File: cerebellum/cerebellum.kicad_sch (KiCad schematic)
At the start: 78 parts, among them J1 PowerIn, J2 UART, J3 SWD_DBG, J4 SWD_DBG_PIN, J5 CAN FD, J6 CAN, Q1 AP2300, U1 OK1061-S, U2 TPS5430DDA, U3 BMI088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

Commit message: [Modify] Complete descriptions in schematics
including cerebellum and heart.
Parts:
- C1, C10, C2, C27, C30, C32, C38, C5, C51, C7: value 100nF, 10%, 10V -> 100nF/10V/0402
- C11, C22, C23, C9: value 100pF, 10%, 10V -> 100pF/1%/50V/0402
- C12, C29, C3, C31, C8: value 4.7uF, 10%, 10V -> 4.7uF/10V/0402
- C13, C16, C18: value 4.7uF 50V -> 4.7uF/50V/0805
- C14: value 10pf 50V -> 10pf/50V/0402
- C15: value 1.5nf 50V -> 1.5nf/50V/0603
- C17: value 10nf 50V -> 10nf/50V/0402
- C19: value 100uf 50V -> 100uf/50V/0805
- C20: value 100nf 10V -> 100nf/10V/0402
- C21: value 1.5nf 50V -> 1.5nf/50V/0402
- C24: value 100nf 50V -> 100nf/50V/0402
- C25: value 10uf 50V -> 10uf/50V/0402
- C26: value 8.2nf 50V -> 8.2nf/50V/0603
- C28: value 150pf 50V -> 150pf/50V/0402
- C33, C36: value 47uf 50V -> 47uf/50V/0603
- C4: value 1uF, 10%, 10V -> 1uF/10V/0402
- C6: value 10uF, 10%, 10V -> 10uF/10V/0402
- D5: value LTST-C281KFKT-5A -> LTST-C281KFKT-5A/0402
- L1, L2, L3: value 15uh, SLO0530H150MTT -> 15uh/SLO0530H150MTT
- R1: value 1k -> 1k/0402
- R10, R6: value 10k -> 10k/0402
- R11: value 549R -> 549R/0201
- R12, R13, R14, R15: value 33R/1% -> 33R/1%/0805
- R16: value 10.2k -> 10.2k/0402
- R17: value 1.96k -> 1.96k/0402
- R2, R8: value 120R -> 120R/0402
- R3: value 64.9k -> 64.9k/0402
- R4: value 169k -> 169k/0402
- R5: value 20.5 -> 20.5/0402
- R7: value 5.9k -> 5.9k/0402
- R9: value 100R -> 100R/0402

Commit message: [Fix] Complete resistor value of 24Vto5V regulator
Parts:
- R5: value 20.5/0402 -> 20.5k/0402
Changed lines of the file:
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@@
       (effects (font (size 1.27 1.27)) (justify right))
     )
-    (property "Value" "20.5/0402" (id 1) (at 294.64 123.19 0)
+    (property "Value" "20.5k/0402" (id 1) (at 294.64 123.19 0)
       (effects (font (size 1.27 1.27)) (justify right))
     )
@@
     )
     (path "/242cc630-7b5d-45c5-9414-a0c5ca6aa299"
-      (reference "R5") (unit 1) (value "20.5/0402") (footprint "Resistor_SMD:R_0402_1005Metric")
+      (reference "R5") (unit 1) (value "20.5k/0402") (footprint "Resistor_SMD:R_0402_1005Metric")
     )
     (path "/f57f7c10-af7d-4f52-88fd-8d7ce55973b5"

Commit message: [Fix] Correct capacities in 24Vto5V converter
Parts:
- C25: value 10uf/50V/0402 -> 10uf/50V/0805; footprint Capacitor_SMD:C_0402_1005Metric -> Capacitor_SMD:C_0805_2012Metric
- C33, C36: value 47uf/50V/0603 -> 47uf/6.3V/0603
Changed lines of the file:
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@@
       (effects (font (size 1.27 1.27)) (justify left))
     )
-    (property "Value" "47uf/50V/0603" (id 1) (at 363.22 124.46 90)
+    (property "Value" "47uf/6.3V/0603" (id 1) (at 363.22 124.46 90)
       (effects (font (size 1.27 1.27)) (justify left))
     )
@@
   (symbol (lib_id "power:GNDA") (at 92.71 77.47 0) (unit 1)
     (in_bom yes) (on_board yes)
-    (property "Reference" "#PWR?" (id 0) (at 92.71 83.82 0)
+    (property "Reference" "#PWR0110" (id 0) (at 92.71 83.82 0)
       (effects (font (size 1.27 1.27)) hide)
     )
@@
       (effects (font (size 1.27 1.27)) (justify left))
     )
-    (property "Value" "47uf/50V/0603" (id 1) (at 370.84 124.46 90)
+    (property "Value" "47uf/6.3V/0603" (id 1) (at 370.84 124.46 90)
       (effects (font (size 1.27 1.27)) (justify left))
     )
@@
       (effects (font (size 1.27 1.27)) (justify left))
     )
-    (property "Value" "10uf/50V/0402" (id 1) (at 283.21 119.38 90)
-      (effects (font (size 1.27 1.27)) (justify left))
-    )
-    (property "Footprint" "Capacitor_SMD:C_0402_1005Metric" (id 2) (at 287.9852 114.3 0)
+    (property "Value" "10uf/50V/0805" (id 1) (at 283.21 119.38 90)
+      (effects (font (size 1.27 1.27)) (justify left))
+    )
+    (property "Footprint" "Capacitor_SMD:C_0805_2012Metric" (id 2) (at 287.9852 114.3 0)
       (effects (font (size 1.27 1.27)) hide)
     )
@@
     )
     (path "/55191d87-ff63-48e6-b782-b5eabc48b1c7"
-      (reference "#PWR?") (unit 1) (value "GNDA") (footprint "")
+      (reference "#PWR0110") (unit 1) (value "GNDA") (footprint "")
     )
     (path "/65313aad-28bf-4519-8673-ecacf3cd8ac6"
@@
     )
     (path "/e787b22a-3d91-4a17-98b9-353fe0181fec"
-      (reference "C25") (unit 1) (value "10uf/50V/0402") (footprint "Capacitor_SMD:C_0402_1005Metric")
+      (reference "C25") (unit 1) (value "10uf/50V/0805") (footprint "Capacitor_SMD:C_0805_2012Metric")
     )
     (path "/93be202b-fdc3-4e76-b2fd-15b6cdae9e2f"
@@
     )
     (path "/0ddd73d0-49e9-4519-8799-16055b6184fb"
-      (reference "C33") (unit 1) (value "47uf/50V/0603") (footprint "Capacitor_SMD:C_0603_1608Metric")
+      (reference "C33") (unit 1) (value "47uf/6.3V/0603") (footprint "Capacitor_SMD:C_0603_1608Metric")
     )
     (path "/d3316d42-63af-4c88-8de1-8da058897181"
-      (reference "C36") (unit 1) (value "47uf/50V/0603") (footprint "Capacitor_SMD:C_0603_1608Metric")
+      (reference "C36") (unit 1) (value "47uf/6.3V/0603") (footprint "Capacitor_SMD:C_0603_1608Metric")
     )
     (path "/0ee1750c-811c-4543-bb64-0d4b8ab140a1"

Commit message: [Modify] Change CAN ports sequence
2pin: 1-CAN_L, 2-CAN_H
3pin: 1-5V, 2-CAN_L, 3-CAN_H
4pin: 1,2-CAN_L, 3,4-CAN_H

Signed-off-by: Homalozoa <nx.tardis@gmail.com>
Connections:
- net CANFD_H: now also J5.2 (Pin_2); no longer J5.1 (Pin_1)
- net CANFD_L: now also J5.1 (Pin_1); no longer J5.2 (Pin_2)
- net CAN_H: now also J6.2 (Pin_2); no longer J6.1 (Pin_1)
- net CAN_L: now also J6.1 (Pin_1); no longer J6.2 (Pin_2)

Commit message: [Fix] Manufacture modification
Signed-off-by: Homalozoa <nx.tardis@gmail.com>
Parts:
- C19: value 100uf/50V/0805 -> 100uf/6.3V/0805
- D3, D4, D6, D7: value 12V -> BV12C
- R11: value 549R/0201 -> 549R/0603; footprint Resistor_SMD:R_0201_0603Metric -> Resistor_SMD:R_0603_1608Metric
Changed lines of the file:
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@@
     (in_bom yes) (on_board yes)
     (property "Reference" "C19" (id 0) (at 334.01 50.8 0))
-    (property "Value" "100uf/50V/0805" (id 1) (at 336.55 55.88 0))
+    (property "Value" "100uf/6.3V/0805" (id 1) (at 336.55 55.88 0))
     (property "Footprint" "Capacitor_SMD:C_0805_2012Metric" (id 2) (at 330.5048 49.53 0)
       (effects (font (size 1.27 1.27)) hide)
@@
       (effects (font (size 1.27 1.27)) (justify right))
     )
-    (property "Value" "12V" (id 1) (at 208.28 238.76 90)
+    (property "Value" "BV12C" (id 1) (at 208.28 238.76 90)
       (effects (font (size 1.27 1.27)) (justify right))
     )
@@
   (symbol (lib_id "Device:R_US") (at 379.73 57.15 0) (mirror y) (unit 1)
     (in_bom yes) (on_board yes) (fields_autoplaced)
-    (property "Reference" "R11" (id 0) (at 377.19 55.8799 0)
-      (effects (font (size 1.27 1.27)) (justify left))
-    )
-    (property "Value" "549R/0201" (id 1) (at 377.19 58.4199 0)
-      (effects (font (size 1.27 1.27)) (justify left))
-    )
-    (property "Footprint" "Resistor_SMD:R_0201_0603Metric" (id 2) (at 378.714 57.404 90)
+    (property "Reference" "R11" (id 0) (at 382.27 55.8799 0)
+      (effects (font (size 1.27 1.27)) (justify right))
+    )
+    (property "Value" "549R/0603" (id 1) (at 382.27 58.4199 0)
+      (effects (font (size 1.27 1.27)) (justify right))
+    )
+    (property "Footprint" "Resistor_SMD:R_0603_1608Metric" (id 2) (at 378.714 57.404 90)
       (effects (font (size 1.27 1.27)) hide)
     )
@@
       (effects (font (size 1.27 1.27)) (justify right))
     )
-    (property "Value" "12V" (id 1) (at 190.5 227.33 90)
+    (property "Value" "BV12C" (id 1) (at 190.5 227.33 90)
       (effects (font (size 1.27 1.27)) (justify right))
     )
@@
       (effects (font (size 1.27 1.27)) (justify right))
     )
-    (property "Value" "12V" (id 1) (at 123.19 226.06 90)
+    (property "Value" "BV12C" (id 1) (at 123.19 226.06 90)
       (effects (font (size 1.27 1.27)) (justify right))
     )
@@
       (effects (font (size 1.27 1.27)) (justify right))
     )
-    (property "Value" "12V" (id 1) (at 140.97 237.49 90)
+    (property "Value" "BV12C" (id 1) (at 140.97 237.49 90)
       (effects (font (size 1.27 1.27)) (justify right))
     )
@@
     )
     (path "/0f6c3a96-c6a2-4cae-b238-f3f5c233b895"
-      (reference "C19") (unit 1) (value "100uf/50V/0805") (footprint "Capacitor_SMD:C_0805_2012Metric")
+      (reference "C19") (unit 1) (value "100uf/6.3V/0805") (footprint "Capacitor_SMD:C_0805_2012Metric")
     )
     (path "/1a81ed92-b7d6-4e2e-b1fa-f759489fe3e3"
@@
     )
     (path "/d6cf48a9-a13f-466f-bfde-8bc93913d1c0"
-      (reference "D3") (unit 1) (value "12V") (footprint "Diode_SMD:D_SOD-323")
+      (reference "D3") (unit 1) (value "BV12C") (footprint "Diode_SMD:D_SOD-323")
     )
     (path "/dca75d67-8d31-4cfe-944d-9a96274d2c81"
-      (reference "D4") (unit 1) (value "12V") (footprint "Diode_SMD:D_SOD-323")
+      (reference "D4") (unit 1) (value "BV12C") (footprint "Diode_SMD:D_SOD-323")
     )
     (path "/a30c0642-d8e5-452a-8e07-4ec5af02c9d7"
@@
     )
     (path "/35231abb-451c-4485-8adf-5fdeff949361"
-      (reference "D6") (unit 1) (value "12V") (footprint "Diode_SMD:D_SOD-323")
+      (reference "D6") (unit 1) (value "BV12C") (footprint "Diode_SMD:D_SOD-323")
     )
     (path "/28d5a148-bc54-44f3-9073-42e0716c8823"
-      (reference "D7") (unit 1) (value "12V") (footprint "Diode_SMD:D_SOD-323")
+      (reference "D7") (unit 1) (value "BV12C") (footprint "Diode_SMD:D_SOD-323")
     )
     (path "/21df13e8-f1cb-4d93-9100-820a610e89e4"
@@
     )
     (path "/2f096358-cf9a-4b82-969d-9875d4f6edad"
-      (reference "R11") (unit 1) (value "549R/0201") (footprint "Resistor_SMD:R_0201_0603Metric")
+      (reference "R11") (unit 1) (value "549R/0603") (footprint "Resistor_SMD:R_0603_1608Metric")
     )
     (path "/8ef88884-2b22-48df-9a58-892a579574e1"

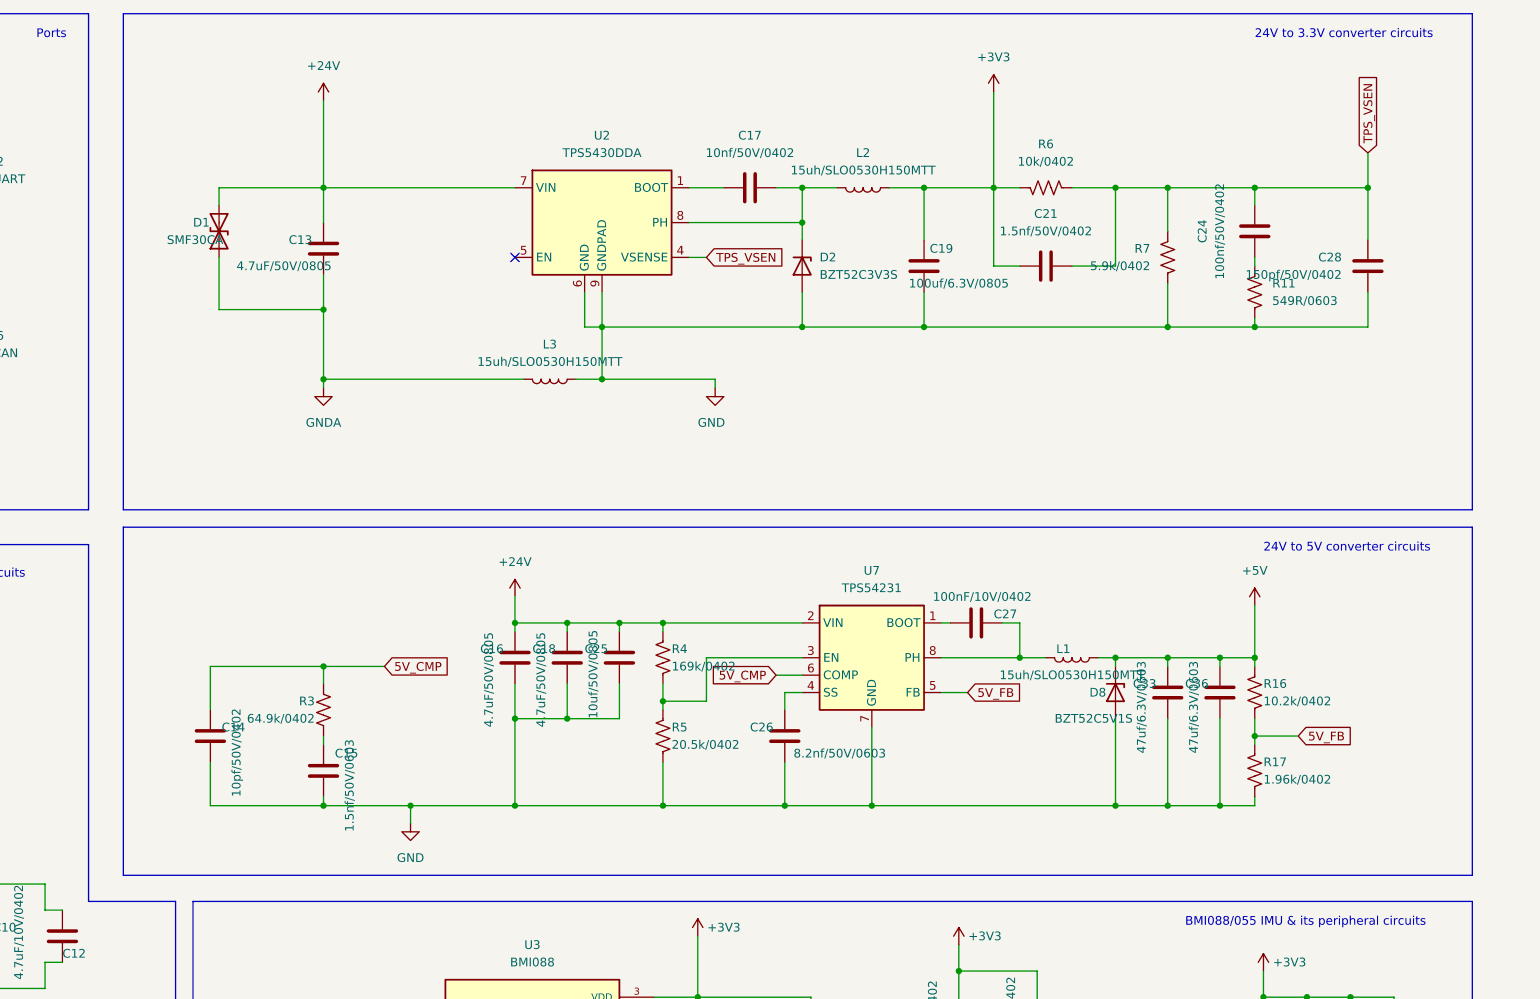
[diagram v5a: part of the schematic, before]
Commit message: [Modify] Replace DCDC(24to3V3) to LDO(5to3V3)
Signed-off-by: Homalozoa <nx.tardis@gmail.com>
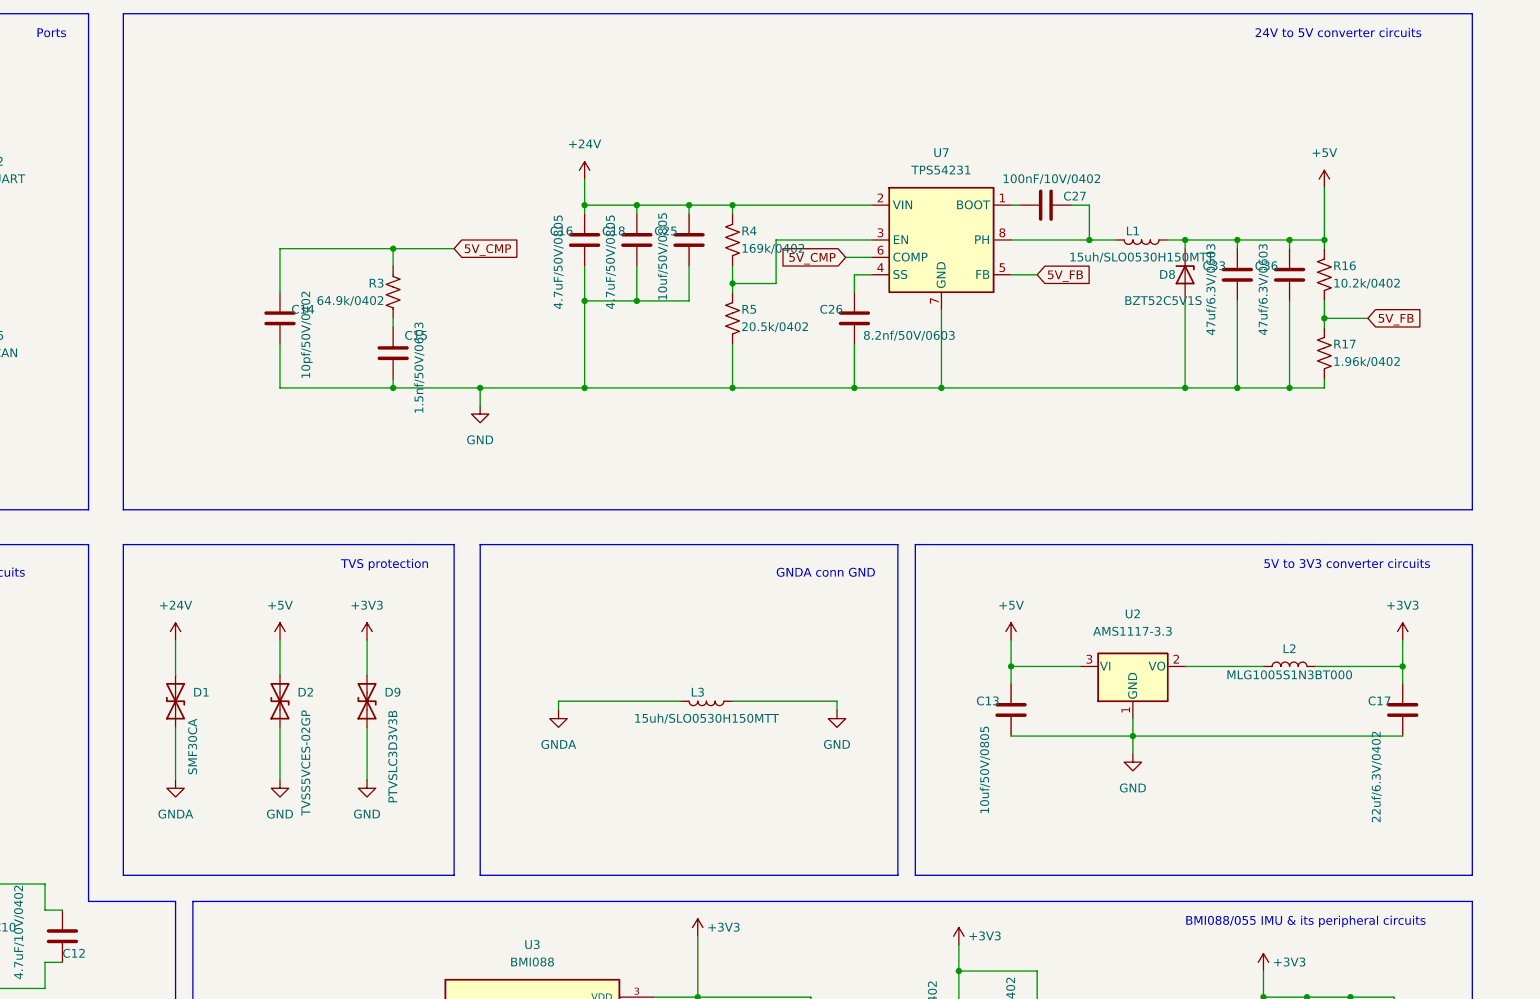
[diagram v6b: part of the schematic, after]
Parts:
- removed C19: 100uf/6.3V/0805, Capacitor_SMD:C_0805_2012Metric, symbol Device:C
- removed C21: 1.5nf/50V/0402, Capacitor_SMD:C_0402_1005Metric, symbol Device:C
- removed C24: 100nf/50V/0402, Capacitor_SMD:C_0402_1005Metric, symbol Device:C
- removed C28: 150pf/50V/0402, Capacitor_SMD:C_0402_1005Metric, symbol Device:C
- removed D2: BZT52C3V3S, Diode_SMD:D_SOD-323, symbol Diode:BZT52Bxx
- removed R11: 549R/0603, Resistor_SMD:R_0603_1608Metric, symbol Device:R_US
- removed R6: 10k/0402, Resistor_SMD:R_0402_1005Metric, symbol Device:R_US
- removed R7: 5.9k/0402, Resistor_SMD:R_0402_1005Metric, symbol Device:R_US
- removed U2: TPS5430DDA, Package_SO:TI_SO-PowerPAD-8_ThermalVias, symbol Regulator_Switching:TPS5430DDA
- added D2: TVSS5VCES-02GP, Diode_SMD:D_SOD-523, symbol Device:D_TVS
- added D9: PTVSLC3D3V3B, Diode_SMD:D_SOD-323, symbol Device:D_TVS
- added U2: AMS1117-3.3, Package_TO_SOT_SMD:SOT-223-3_TabPin2, symbol Regulator_Linear:AMS1117-3.3
- C13: value 4.7uF/50V/0805 -> 10uf/50V/0805
- C17: value 10nf/50V/0402 -> 22uf/6.3V/0402
- L2: value 15uh/SLO0530H150MTT -> MLG1005S1N3BT000; footprint Inductor_SMD:L_Sunlord_MWSA0518_5.4x5.2mm -> Inductor_SMD:L_0402_1005Metric
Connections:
- net +24V: no longer C13.1
- net +3V3: now also C17.1, L2.2, D9.2 (A2); no longer L2.1
- net +5V: now also C13.1, D2.2 (A2), U2.3 (VI)
- net GND: now also C13.2, C17.2, D2.1 (A1), D9.1 (A1), U2.1 (GND)
- net GNDA: no longer C13.2
- new net: L2.1, U2.2 (VO)
- no-connect marks 70 -> 69
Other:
- note added: "5V to 3V3 converter circuits"
- note added: "GNDA conn GND"
- note added: "TVS protection"
- note removed: "24V to 3.3V converter circuits"
- moved on the sheet: C14, C15, C16, C18, C25, C26, C27, C33, C36, D8, L1, R16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
